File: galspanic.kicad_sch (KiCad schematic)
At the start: 24 parts, among them J1 x68000_expansion, U1 CY62167E, U10 SN74AHCT245, U11 SN74AHCT245, U2 CY62167E, U3 CY62167E, U4 CY62167E, U5 ATF22V10C-10PU, U6 SN74AHCT245, U7 SN74AHCT245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

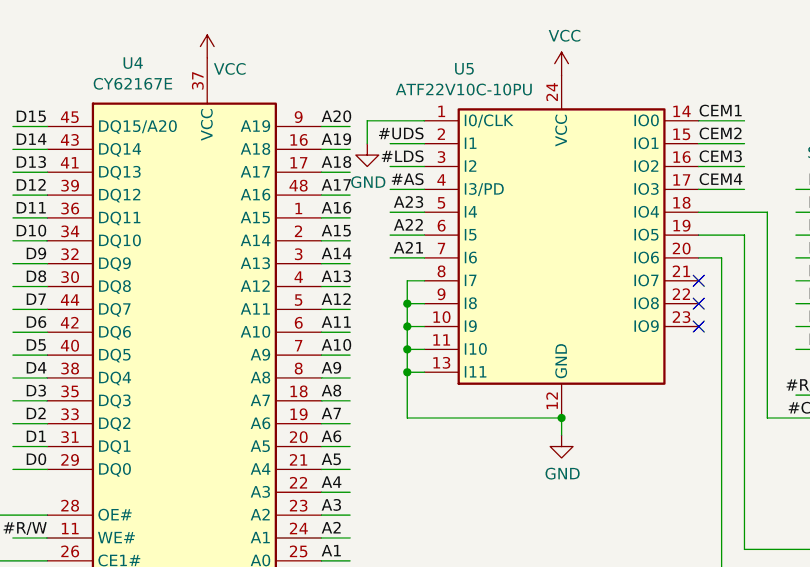
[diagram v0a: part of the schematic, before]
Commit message: route A20, fix power cap footprint
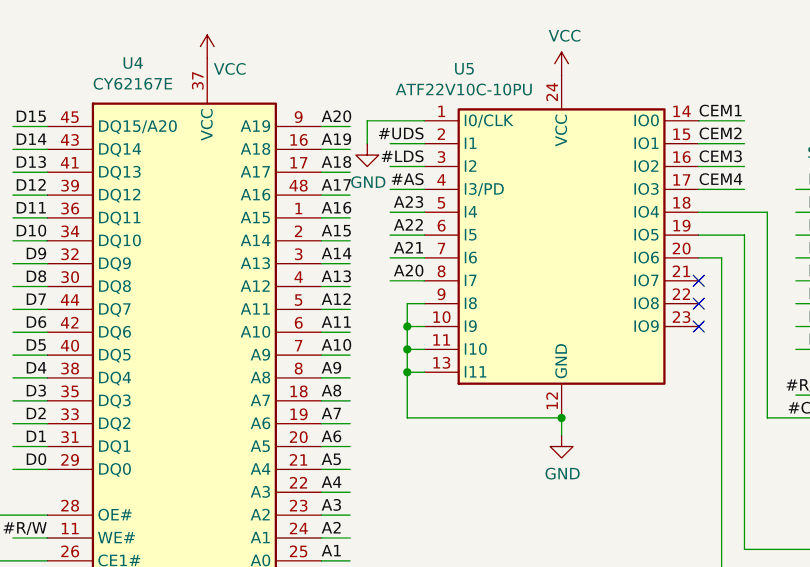
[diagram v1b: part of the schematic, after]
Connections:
- net A20: now also U5.8 (I7)
- net GND: no longer U5.8 (I7)
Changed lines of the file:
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@@
   (junction (at 112.395 184.785))
   (junction (at 112.395 189.865))
-  (junction (at 113.03 130.81))
   (junction (at 113.03 133.35))
   (junction (at 113.03 135.89))
@@
   (junction (at 238.76 151.765))
   (junction (at 280.67 149.225))
-  (no_connect (at 273.05 136.525))
-  (no_connect (at 273.05 103.505))
+  (no_connect (at 145.415 130.81))
   (no_connect (at 273.05 100.965))
-  (no_connect (at 273.05 121.285))
-  (no_connect (at 145.415 133.35))
-  (no_connect (at 273.05 126.365))
-  (no_connect (at 273.05 144.145))
-  (no_connect (at 145.415 130.81))
-  (no_connect (at 273.05 141.605))
-  (no_connect (at 200.025 83.82))
-  (no_connect (at 273.05 116.205))
   (no_connect (at 273.05 32.385))
-  (no_connect (at 273.05 133.985))
-  (no_connect (at 145.415 128.27))
-  (no_connect (at 273.05 139.065))
-  (no_connect (at 273.05 123.825))
-  (no_connect (at 273.05 146.685))
-  (no_connect (at 273.05 106.045))
   (no_connect (at 273.05 131.445))
   (no_connect (at 273.05 118.745))
+  (no_connect (at 273.05 126.365))
   (no_connect (at 273.05 108.585))
+  (no_connect (at 200.025 83.82))
+  (no_connect (at 273.05 103.505))
+  (no_connect (at 145.415 133.35))
+  (no_connect (at 273.05 146.685))
   (no_connect (at 273.05 29.845))
+  (no_connect (at 273.05 141.605))
+  (no_connect (at 200.025 86.36))
+  (no_connect (at 273.05 116.205))
+  (no_connect (at 273.05 106.045))
+  (no_connect (at 273.05 123.825))
   (no_connect (at 273.05 113.665))
+  (no_connect (at 273.05 144.145))
   (no_connect (at 200.025 88.9))
-  (no_connect (at 200.025 86.36))
+  (no_connect (at 273.05 139.065))
+  (no_connect (at 145.415 128.27))
+  (no_connect (at 273.05 133.985))
+  (no_connect (at 273.05 121.285))
+  (no_connect (at 273.05 34.925))
+  (no_connect (at 273.05 136.525))
   (no_connect (at 273.05 111.125))
-  (no_connect (at 273.05 34.925))
   (wire (pts (xy 18.415 66.675) (xy 18.415 71.755)))
   (wire (pts (xy 18.415 71.755) (xy 18.415 86.995)))
@@
   (wire (pts (xy 111.125 123.19) (xy 114.935 123.19)))
   (wire (pts (xy 111.125 125.73) (xy 114.935 125.73)))
+  (wire (pts (xy 111.125 128.27) (xy 114.935 128.27)))
   (wire (pts (xy 112.395 184.785) (xy 118.745 184.785)))
   (wire (pts (xy 112.395 189.865) (xy 118.745 189.865)))
-  (wire (pts (xy 113.03 128.27) (xy 113.03 130.81)))
   (wire (pts (xy 113.03 130.81) (xy 113.03 133.35)))
   (wire (pts (xy 113.03 130.81) (xy 114.935 130.81)))
@@
   (wire (pts (xy 113.03 143.51) (xy 130.175 143.51)))
   (wire (pts (xy 114.935 110.49) (xy 108.585 110.49)))
-  (wire (pts (xy 114.935 128.27) (xy 113.03 128.27)))
   (wire (pts (xy 118.745 184.785) (xy 125.095 184.785)))
   (wire (pts (xy 118.745 189.865) (xy 125.095 189.865)))
@@
     (effects (font (size 1.27 1.27)) (justify right bottom))
   )
+  (label "A20" (at 114.935 128.27 180)
+    (effects (font (size 1.27 1.27)) (justify right bottom))
+  )

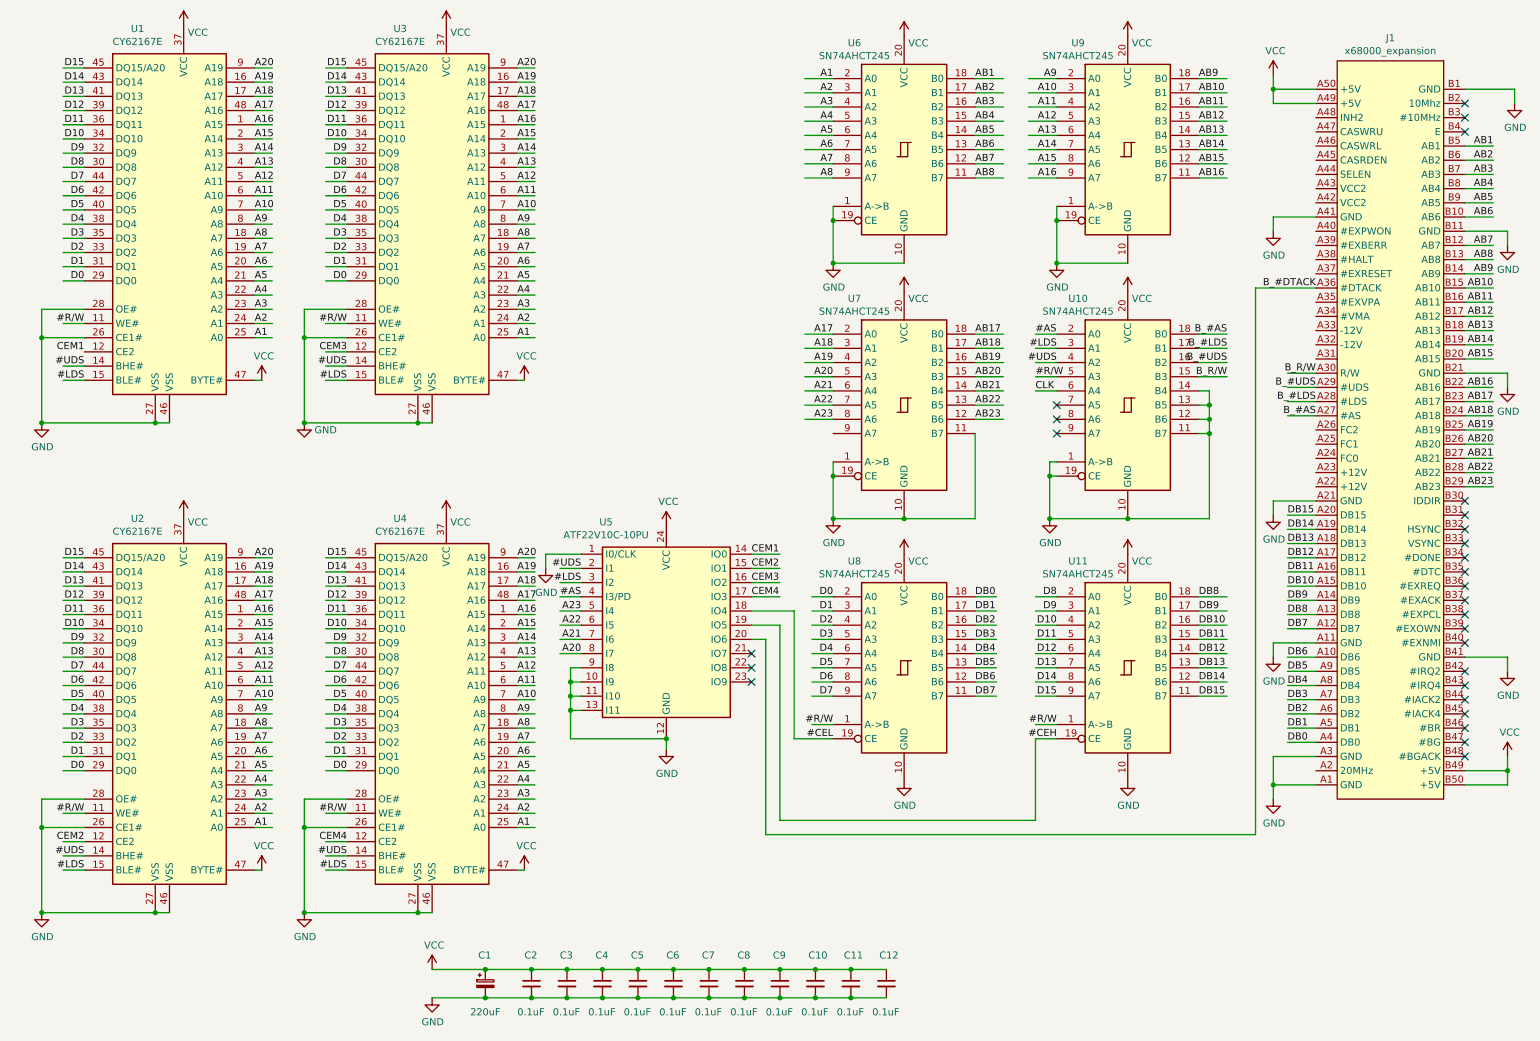
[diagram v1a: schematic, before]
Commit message: pcb: add memory size jumpers
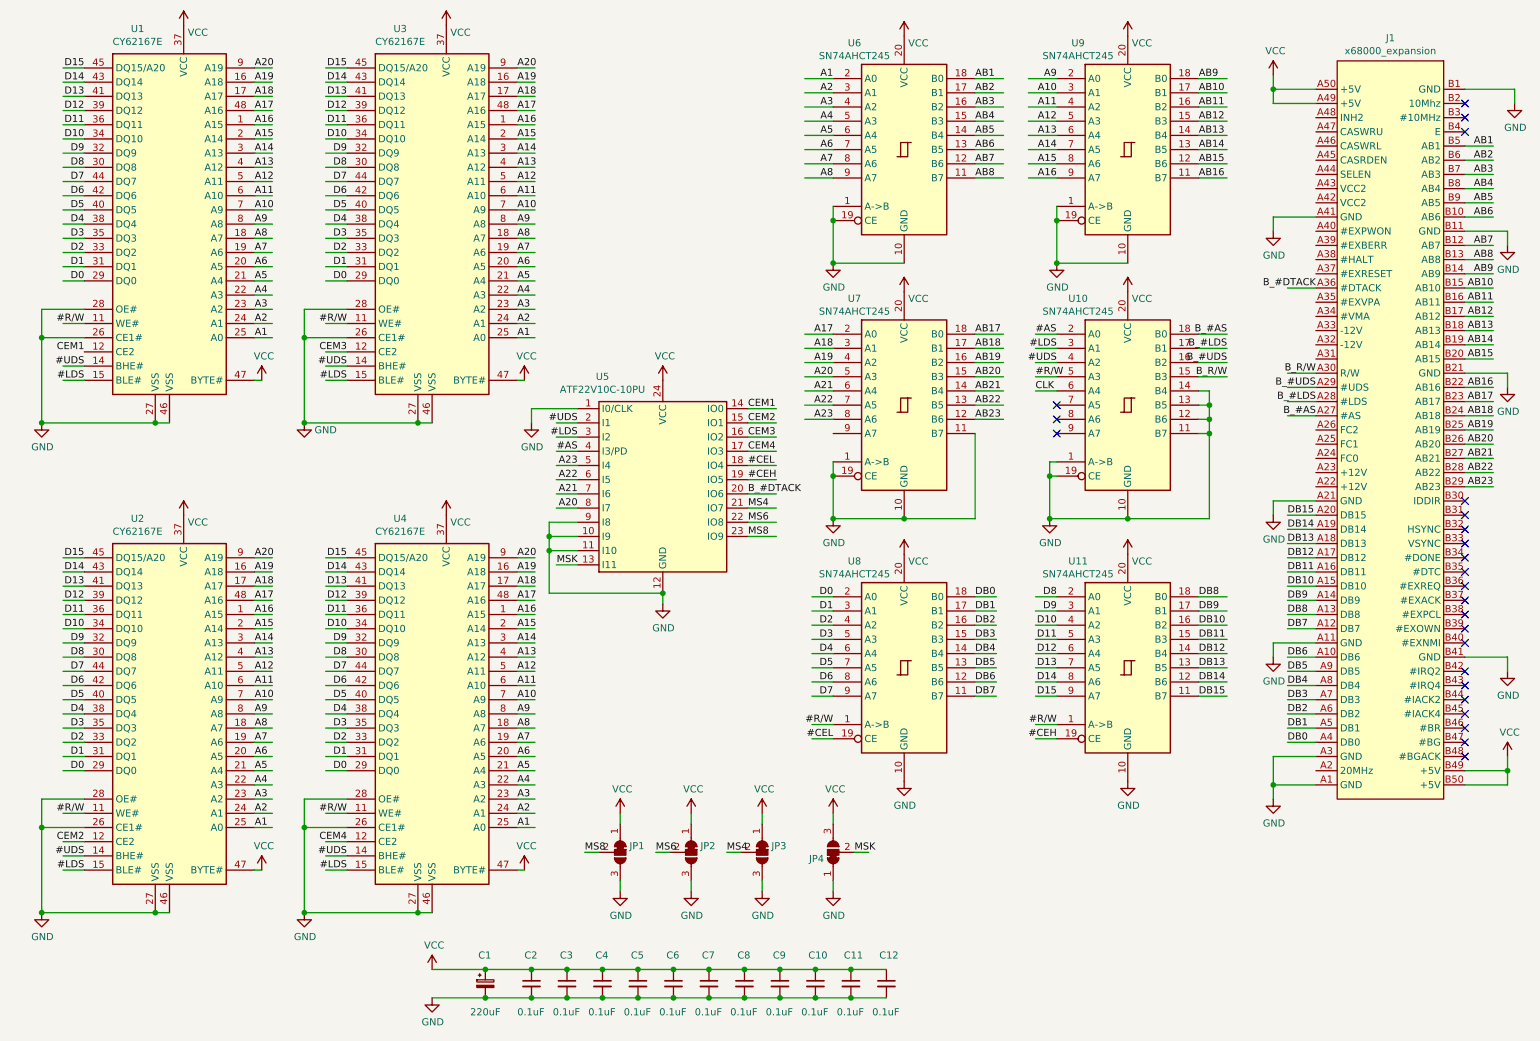
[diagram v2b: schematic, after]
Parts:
- added JP1, JP2, JP3, JP4: SolderJumper_3_Bridged12, Jumper:SolderJumper-3_P1.3mm_Bridged12_RoundedPad1.0x1.5mm, symbol Jumper:SolderJumper_3_Bridged12
- C1: footprint Capacitor_THT:CP_Radial_D8.0mm_P5.00mm -> Capacitor_THT:CP_Radial_D6.3mm_P2.50mm
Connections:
- net GND: now also JP1.3 (B), JP2.3 (B), JP3.3 (B), JP4.1 (A); no longer U5.13 (I11)
- net VCC: now also JP1.1 (A), JP2.1 (A), JP3.1 (A), JP4.3 (B)
- net MS4: now reaches U5.21 (IO7)
- net MS4: now also JP3.2 (C)
- net MS6: now reaches U5.22 (IO8)
- net MS6: now also JP2.2 (C)
- net MS8: now reaches U5.23 (IO9)
- net MS8: now also JP1.2 (C)
- new net MSK: JP4.2 (C), U5.13 (I11)
- no-connect marks 27 -> 24
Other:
- moved on the sheet: U5

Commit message: release a smaller board with no buffers
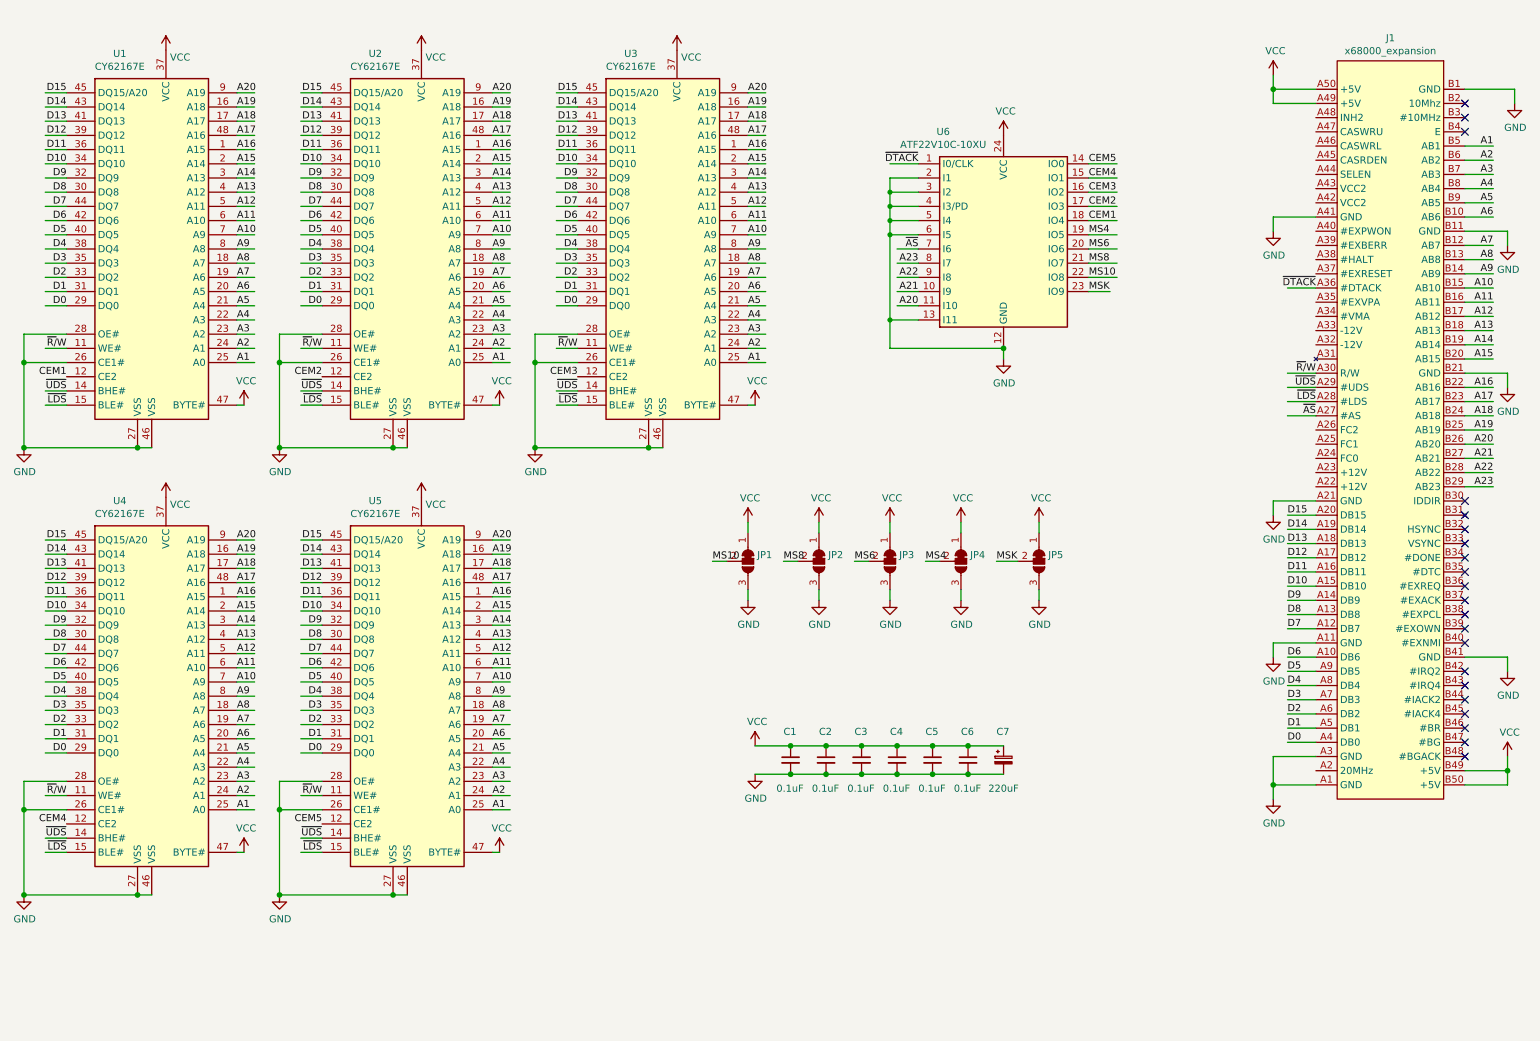
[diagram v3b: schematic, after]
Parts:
- removed C10, C11, C12, C8, C9: 0.1uF, Capacitor_SMD:C_0603_1608Metric_Pad1.05x0.95mm_HandSolder, symbol Device:C_Small
- removed U10, U11, U6, U7, U8, U9: SN74AHCT245, Package_SO:SOIC-20W_7.5x12.8mm_P1.27mm, symbol galspanic:SN74AHCT245
- added JP1: SolderJumper_3_Bridged12, Jumper:SolderJumper-3_P1.3mm_Bridged12_RoundedPad1.0x1.5mm, symbol Jumper:SolderJumper_3_Bridged12
- added U5: CY62167E, Package_SO:TSOP-I-48_18.4x12mm_P0.5mm, symbol galspanic:CY62167E
- C1: renamed from C7; footprint Capacitor_SMD:C_0603_1608Metric_Pad1.05x0.95mm_HandSolder -> Capacitor_SMD:C_0603_1608Metric_Pad1.08x0.95mm_HandSolder
- C2, C3, C4, C5, C6: footprint Capacitor_SMD:C_0603_1608Metric_Pad1.05x0.95mm_HandSolder -> Capacitor_SMD:C_0603_1608Metric_Pad1.08x0.95mm_HandSolder
- U6: renamed from U5; value ATF22V10C-10PU -> ATF22V10C-10XU; footprint Package_DIP:DIP-24_W7.62mm -> Package_SO:TSSOP-24_4.4x7.8mm_P0.65mm
- renumbered C1 to C7, JP1 to JP2, JP2 to JP3, JP3 to JP4, JP4 to JP5
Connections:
- net #AS is gone; now on net GND: U6.4 (I3/PD)
- net #CEH is gone; now on net MS4: U6.19 (IO5)
- net #CEL is gone; now on net CEM1: U6.18 (IO4)
- net AB1 is gone; now on net A1: J1.B5 (AB1)
- net AB10 is gone; now on net A10: J1.B15 (AB10)
- net AB11 is gone; now on net A11: J1.B16 (AB11)
- net AB12 is gone; now on net A12: J1.B17 (AB12)
- net AB13 is gone; now on net A13: J1.B18 (AB13)
- net AB14 is gone; now on net A14: J1.B19 (AB14)
- net AB15 is gone; now on net A15: J1.B20 (AB15)
- net AB16 is gone; now on net A16: J1.B22 (AB16)
- net AB17 is gone; now on net A17: J1.B23 (AB17)
- net AB18 is gone; now on net A18: J1.B24 (AB18)
- net AB19 is gone; now on net A19: J1.B25 (AB19)
- net AB2 is gone; now on net A2: J1.B6 (AB2)
- net AB20 is gone; now on net A20: J1.B26 (AB20)
- net AB21 is gone; now on net A21: J1.B27 (AB21)
- net AB22 is gone; now on net A22: J1.B28 (AB22)
- net AB23 is gone; now on net A23: J1.B29 (AB23)
- net AB3 is gone; now on net A3: J1.B7 (AB3)
- net AB4 is gone; now on net A4: J1.B8 (AB4)
- net AB5 is gone; now on net A5: J1.B9 (AB5)
- net AB6 is gone; now on net A6: J1.B10 (AB6)
- net AB7 is gone; now on net A7: J1.B12 (AB7)
- net AB8 is gone; now on net A8: J1.B13 (AB8)
- net AB9 is gone; now on net A9: J1.B14 (AB9)
- net B_#LDS is gone; now on net ~{LDS}: J1.A28 (#LDS)
- net B_#UDS is gone; now on net ~{UDS}: J1.A29 (#UDS)
- net B_R/W is gone; now on net ~{R/}W: J1.A30 (R/W)
- net DB0 is gone; now on net D0: J1.A4 (DB0)
- net DB1 is gone; now on net D1: J1.A5 (DB1)
- net DB10 is gone; now on net D10: J1.A15 (DB10)
- net DB11 is gone; now on net D11: J1.A16 (DB11)
- net DB12 is gone; now on net D12: J1.A17 (DB12)
- net DB13 is gone; now on net D13: J1.A18 (DB13)
- net DB14 is gone; now on net D14: J1.A19 (DB14)
- net DB15 is gone; now on net D15: J1.A20 (DB15)
- net DB2 is gone; now on net D2: J1.A6 (DB2)
- net DB3 is gone; now on net D3: J1.A7 (DB3)
- net DB4 is gone; now on net D4: J1.A8 (DB4)
- net DB5 is gone; now on net D5: J1.A9 (DB5)
- net DB6 is gone; now on net D6: J1.A10 (DB6)
- net DB7 is gone; now on net D7: J1.A12 (DB7)
- net DB8 is gone; now on net D8: J1.A13 (DB8)
- net DB9 is gone; now on net D9: J1.A14 (DB9)
- net A1: now also U5.25 (A0)
- net A10: now also U5.7 (A9)
- net A11: now also U5.6 (A10)
- net A12: now also U5.5 (A11)
- net A13: now also U5.4 (A12)
- net A14: now also U5.3 (A13)
- net A15: now also U5.2 (A14)
- net A16: now also U5.1 (A15)
- net A17: now also U5.48 (A16)
- net A18: now also U5.17 (A17)
- net A19: now also U5.16 (A18)
- net A2: now also U5.24 (A1)
- net A20: now also U6.11 (I10), U5.9 (A19); no longer U6.8 (I7)
- net A21: now also U6.10 (I9); no longer U6.7 (I6)
- net A22: now also U6.9 (I8); no longer U6.6 (I5)
- net A23: now also U6.8 (I7); no longer U6.5 (I4)
- net A3: now also U5.23 (A2)
- net A4: now also U5.22 (A3)
- net A5: now also U5.21 (A4)
- net A6: now also U5.20 (A5)
- net A7: now also U5.19 (A6)
- net A8: now also U5.18 (A7)
- net A9: now also U5.8 (A8)
- net CEM1: no longer U6.14 (IO0)
- net CEM2: now also U6.17 (IO3); no longer U6.15 (IO1)
- net CEM4: now also U6.15 (IO1); no longer U6.17 (IO3)
- net D0: now also U5.29 (DQ0)
- net D1: now also U5.31 (DQ1)
- net D10: now also U5.34 (DQ10)
- net D11: now also U5.36 (DQ11)
- net D12: now also U5.39 (DQ12)
- net D13: now also U5.41 (DQ13)
- net D14: now also U5.43 (DQ14)
- net D15: now also U5.45 (DQ15/A20)
- net D2: now also U5.33 (DQ2)
- net D3: now also U5.35 (DQ3)
- net D4: now also U5.38 (DQ4)
- net D5: now also U5.40 (DQ5)
- net D6: now also U5.42 (DQ6)
- net D7: now also U5.44 (DQ7)
- net D8: now also U5.30 (DQ8)
- net D9: now also U5.32 (DQ9)
- net GND: now also JP5.3 (B), U6.13 (I11), U6.2 (I1), U6.3 (I2), U6.5 (I4), U6.6 (I5), JP1.3 (B), U5.26 (CE1#), U5.27 (VSS), U5.28 (OE#), U5.46 (VSS); no longer JP5.1 (A), U6.1 (I0/CLK), U6.10 (I9), U6.11 (I10), U6.9 (I8)
- net MS4: no longer U6.21 (IO7)
- net MS6: now also U6.20 (IO6); no longer U6.22 (IO8)
- net MS8: now also U6.21 (IO7); no longer U6.23 (IO9)
- net MSK: now also U6.23 (IO9); no longer U6.13 (I11)
- net VCC: now also JP5.1 (A), JP1.1 (A), U5.37 (VCC), U5.47 (BYTE#); no longer JP5.3 (B)
- net #LDS renamed ~{LDS}
- net ~{LDS}: now also U5.15 (BLE#); no longer U6.3 (I2)
- net #R/W renamed ~{R/}W
- net ~{R/}W: now also U5.11 (WE#)
- net #UDS renamed ~{UDS}
- net ~{UDS}: now also U5.14 (BHE#); no longer U6.2 (I1)
- net B_#AS renamed ~{AS}
- net ~{AS}: now also U6.7 (I6)
- net B_#DTACK renamed ~{DTACK}
- net ~{DTACK}: now also U6.1 (I0/CLK); no longer U6.20 (IO6)
- new net CEM5: U5.12 (CE2), U6.14 (IO0)
- new net MS10: JP1.2 (C), U6.22 (IO8)
- no-connect marks 24 -> 21
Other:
- moved on the sheet: C1, C2, C3, C4, C5, C6, C7, JP2, JP3, JP4, JP5, U1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
